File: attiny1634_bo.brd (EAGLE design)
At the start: 49.5 x 22.2 mm, 13 parts, among them J1 AVR_SPI_PRG_6NS, Y1 12MHz

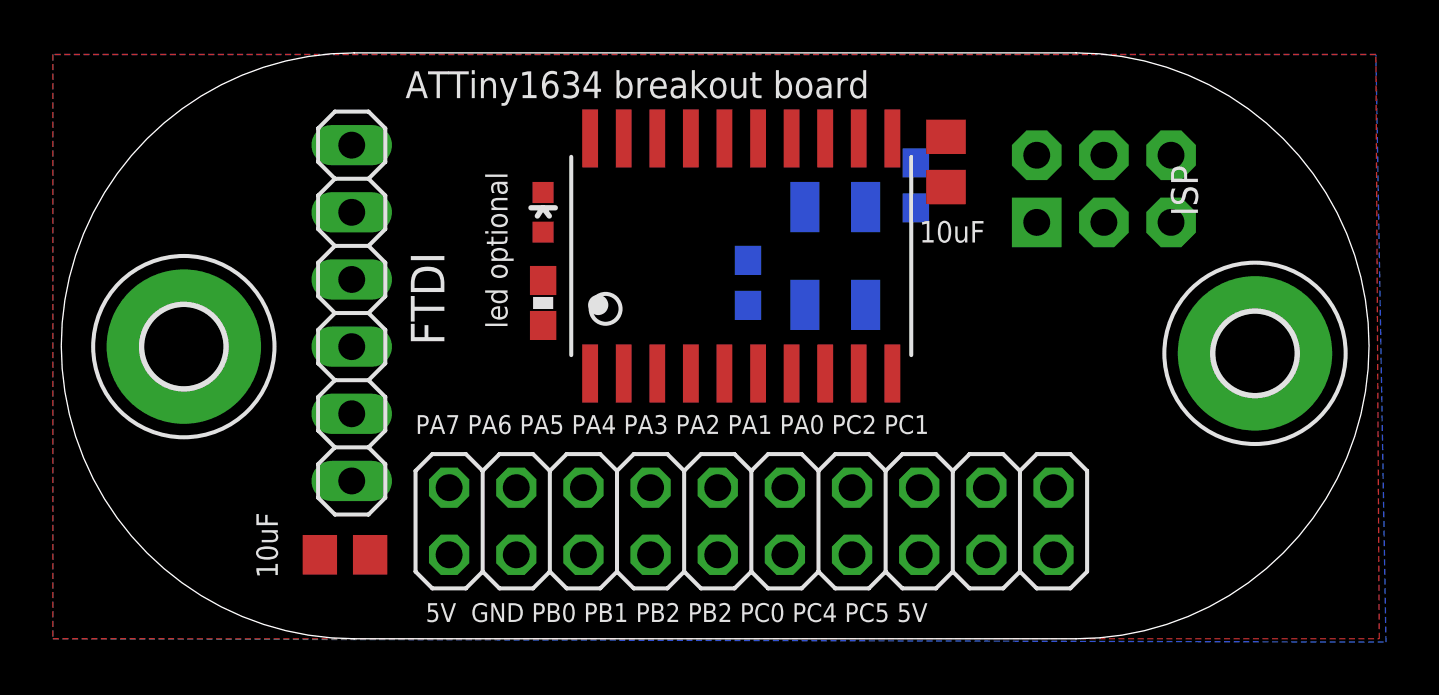
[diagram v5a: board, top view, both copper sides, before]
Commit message: added Arduino style FTDI UART header
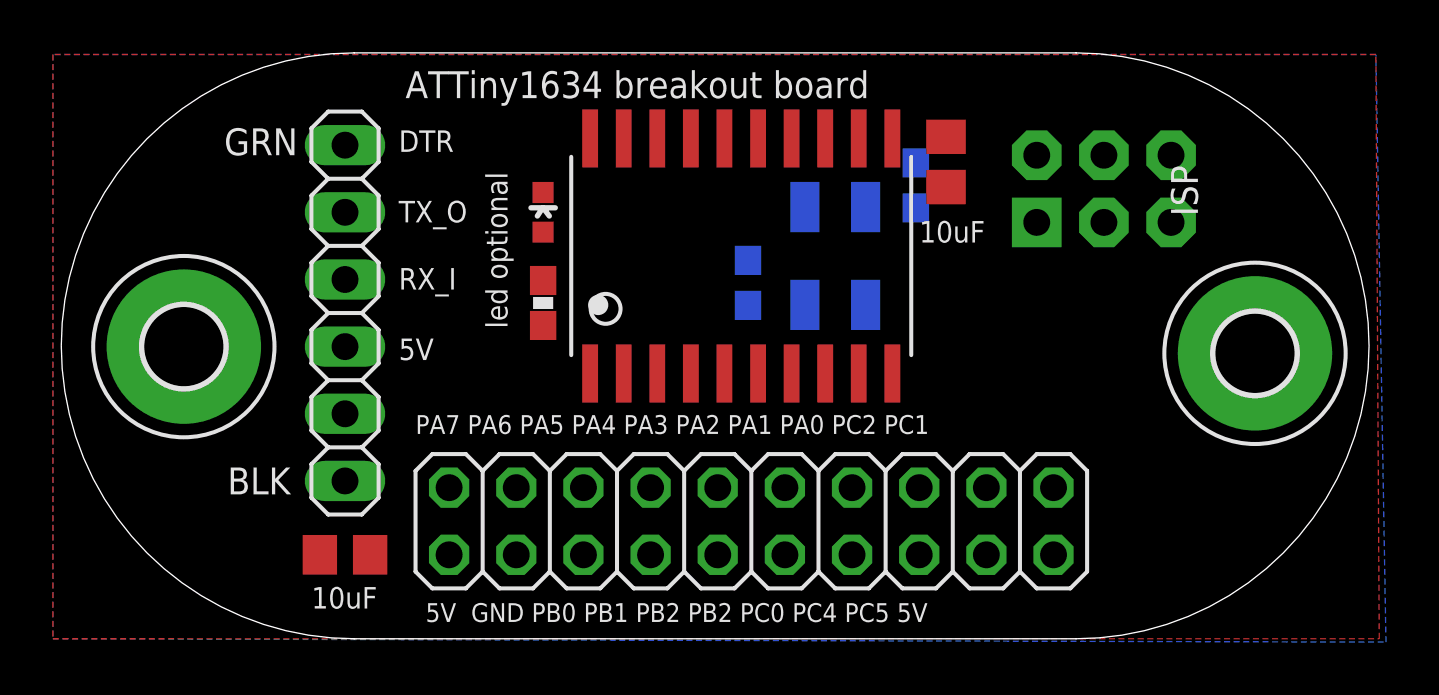
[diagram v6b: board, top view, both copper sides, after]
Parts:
- moved FTDI 0.25 mm to (11.0, 12.3)
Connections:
- removed net PA7: JP1.19
- new net CTS: FTDI.2
- new net PA7/RX0: FTDI.4, JP1.19
- net +5V: now also FTDI.3
- net GND: now also FTDI.1
- net PB0/TXD0: now also FTDI.5
- net PC3/-RESET: now also FTDI.6
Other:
- board text added: "5V"
- board text added: "BLK"
- board text added: "DTR"
- board text added: "GRN"
- board text added: "RX_I"
- board text added: "TX_O"
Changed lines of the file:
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@@
 <text x="27.432" y="16.51" size="0.8128" layer="26" font="vector" ratio="10" rot="MR0">XTAL optional (12MHz)</text>
 <text x="16.383" y="17.653" size="0.8128" layer="25" font="vector" ratio="10" rot="R270">led optional</text>
-<text x="8.509" y="2.286" size="0.8128" layer="25" font="vector" ratio="10" rot="R90">10uF</text>
+<text x="9.779" y="1.143" size="0.8128" layer="25" font="vector" ratio="10">10uF</text>
 <text x="32.766" y="14.986" size="0.8128" layer="25" font="vector" ratio="10">10uF</text>
 <text x="25.781" y="15.367" size="0.8128" layer="26" ratio="10" rot="MR0">12pF caps for xtal</text>
 <circle x="20.6248" y="12.6238" radius="0.179603125" width="0.4064" layer="25"/>
+<text x="6.477" y="18.288" size="1.016" layer="25" ratio="10">GRN</text>
+<text x="6.604" y="5.461" size="1.016" layer="25" ratio="10">BLK</text>
+<text x="13.081" y="18.415" size="0.8128" layer="25" ratio="10">DTR</text>
+<text x="13.081" y="15.748" size="0.8128" layer="25" ratio="10">TX_O</text>
+<text x="13.081" y="13.208" size="0.8128" layer="25" ratio="10">RX_I</text>
+<text x="13.081" y="10.541" size="0.8128" layer="25" ratio="10">5V</text>
 </plain>
 <attributes>
@@
 <element name="U$1" library="attiny1634" package="SOIC20" value="ATTINY1634" x="22.225" y="14.478" smashed="yes"/>
 <element name="RLED1" library="SparkFun-Passives" package="0603-RES" value="330" x="18.542" y="12.7" smashed="yes" rot="R270"/>
-<element name="FTDI" library="pinhead" package="1X06" value="" x="11.303" y="12.319" smashed="yes" rot="R90">
-<attribute name="NAME" x="14.8082" y="11.0998" size="1.27" layer="25" ratio="10" rot="R90"/>
-<attribute name="VALUE" x="14.478" y="4.699" size="1.27" layer="27" rot="R90"/>
+<element name="FTDI" library="pinhead" package="1X06" value="" x="11.049" y="12.319" smashed="yes" rot="R90">
+<attribute name="VALUE" x="14.224" y="4.699" size="1.27" layer="27" rot="R90"/>
 </element>
 </elements>
@@
 <contactref element="U$1" pad="10"/>
 <contactref element="U$1" pad="10"/>
+<contactref element="FTDI" pad="1"/>
 </signal>
 <signal name="+5V" class="1">
@@
 <contactref element="U$1" pad="11"/>
 <contactref element="RLED1" pad="2"/>
+<contactref element="FTDI" pad="3"/>
 <wire x1="33.782" y1="18.984" x2="37.211" y2="18.288" width="0" layer="19" extent="1-1"/>
 <wire x1="31.75" y1="18.923" x2="33.782" y2="18.984" width="0" layer="19" extent="1-1"/>
 <wire x1="18.542" y1="11.85" x2="31.75" y2="18.923" width="0" layer="19" extent="1-1"/>
-<wire x1="14.986" y1="3.175" x2="18.542" y2="11.85" width="0" layer="19" extent="1-1"/>
-<wire x1="11.999" y1="3.175" x2="14.986" y2="3.175" width="0" layer="19" extent="1-1"/>
+<wire x1="11.049" y1="11.049" x2="18.542" y2="11.85" width="0" layer="19" extent="1-1"/>
+<wire x1="11.999" y1="3.175" x2="11.049" y2="11.049" width="0" layer="19" extent="1-1"/>
+<wire x1="14.986" y1="3.175" x2="11.999" y2="3.175" width="0" layer="19" extent="1-1"/>
 <wire x1="37.846" y1="3.175" x2="37.211" y2="18.288" width="0" layer="19" extent="1-1"/>
 </signal>
@@
 <contactref element="J1" pad="5"/>
 <contactref element="U$1" pad="14"/>
+<contactref element="FTDI" pad="6"/>
 <wire x1="27.94" y1="18.923" x2="42.291" y2="15.748" width="0" layer="19" extent="1-1"/>
+<wire x1="11.049" y1="18.669" x2="27.94" y2="18.923" width="0" layer="19" extent="1-1"/>
 </signal>
 <signal name="PC5/XTAL1">
@@
 <contactref element="JP1" pad="9"/>
 </signal>
-<signal name="PA7">
+<signal name="PA7/RX0">
 <contactref element="JP1" pad="19"/>
+<contactref element="FTDI" pad="4"/>
+<wire x1="14.986" y1="5.715" x2="11.049" y2="13.589" width="0" layer="19" extent="1-1"/>
 </signal>
 <signal name="PA6">
@@
 <signal name="PB0/TXD0">
 <contactref element="U$1" pad="1"/>
+<contactref element="FTDI" pad="5"/>
+<wire x1="11.049" y1="16.129" x2="20.32" y2="10.033" width="0" layer="19" extent="1-1"/>
 </signal>
 <signal name="PB1/MOSI/ADC6">
@@
 <wire x1="18.542" y1="13.55" x2="18.542" y2="15.379" width="0" layer="19" extent="1-1"/>
 </signal>
+<signal name="CTS">
+<contactref element="FTDI" pad="2"/>
+</signal>
 </signals>

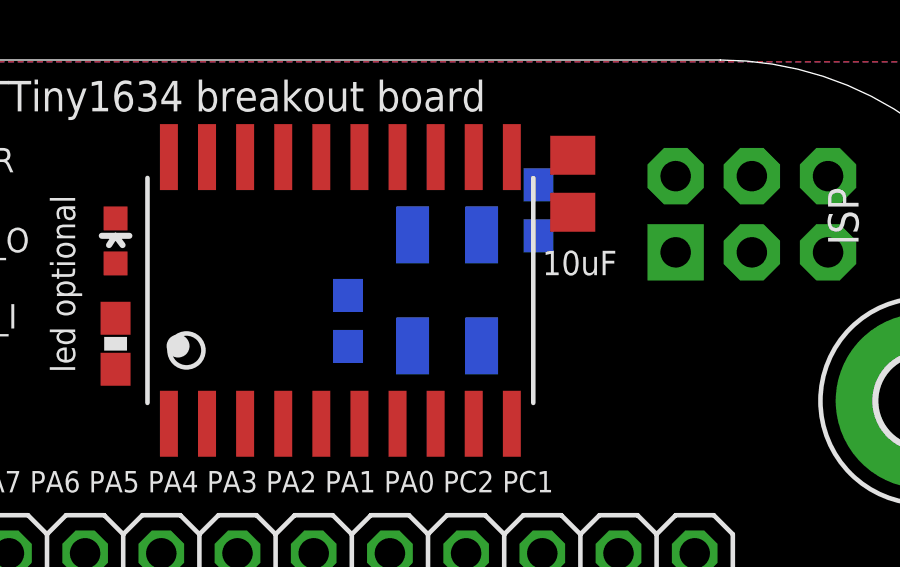
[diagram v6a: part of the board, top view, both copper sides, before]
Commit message: manually routed the xtal
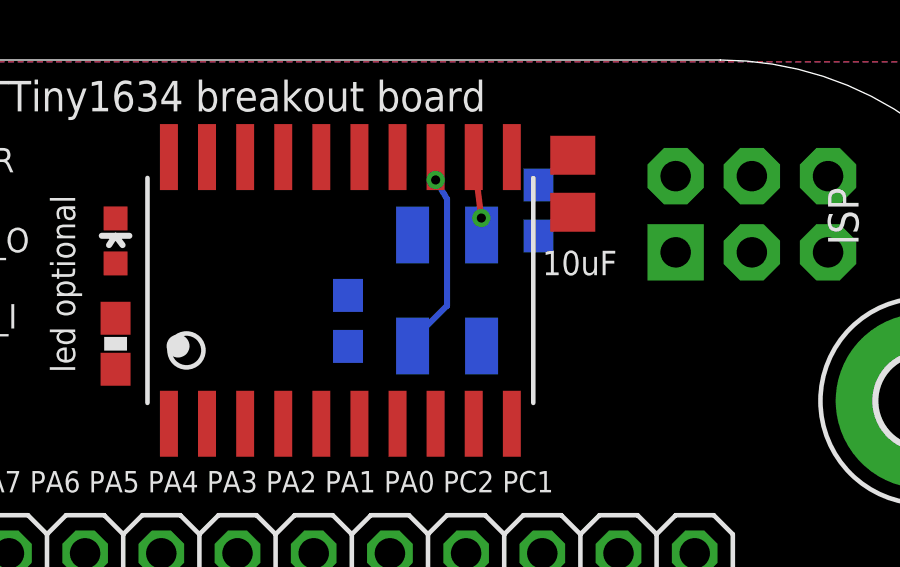
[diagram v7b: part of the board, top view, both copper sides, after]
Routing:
- net PC4/XTAL2: track 0.00 -> 6.88 mm, vias 0 -> 1
- net PC5/XTAL1: track 0.00 -> 2.81 mm, vias 0 -> 1
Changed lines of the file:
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@@
 <contactref element="JP1" pad="4"/>
 <contactref element="U$1" pad="12"/>
-<wire x1="30.741" y1="16.328" x2="30.48" y2="18.923" width="0" layer="19" extent="1-16"/>
-<wire x1="32.639" y1="16.295" x2="30.741" y2="16.328" width="0" layer="19" extent="16-16"/>
+<wire x1="30.48" y1="18.923" x2="30.734" y2="16.891" width="0.2032" layer="1"/>
+<via x="30.734" y="16.891" extent="1-16" drill="0.3048"/>
+<wire x1="30.734" y1="16.891" x2="30.48" y2="16.589" width="0.2032" layer="16"/>
+<wire x1="30.48" y1="16.589" x2="30.741" y2="16.328" width="0.2032" layer="16"/>
+<wire x1="30.741" y1="16.328" x2="32.639" y2="16.295" width="0" layer="19" extent="16-16"/>
 <wire x1="35.306" y1="3.175" x2="32.639" y2="16.295" width="0" layer="19" extent="16-16"/>
 </signal>
@@
 <contactref element="JP1" pad="6"/>
 <contactref element="U$1" pad="13"/>
-<wire x1="28.441" y1="12.628" x2="29.21" y2="18.923" width="0" layer="19" extent="1-16"/>
-<wire x1="26.289" y1="12.612" x2="28.441" y2="12.628" width="0" layer="19" extent="16-16"/>
+<wire x1="28.441" y1="12.628" x2="28.441" y2="12.82" width="0.2032" layer="16"/>
+<wire x1="28.441" y1="12.82" x2="29.591" y2="13.97" width="0.2032" layer="16"/>
+<wire x1="29.591" y1="13.97" x2="29.591" y2="17.526" width="0.2032" layer="16"/>
+<wire x1="29.591" y1="17.526" x2="29.21" y2="18.161" width="0.2032" layer="16"/>
+<wire x1="29.21" y1="18.923" x2="29.21" y2="18.161" width="0.2032" layer="1"/>
+<via x="29.21" y="18.161" extent="1-16" drill="0.3048"/>
+<wire x1="26.289" y1="12.612" x2="28.441" y2="12.82" width="0" layer="19" extent="16-16"/>
 <wire x1="32.766" y1="3.175" x2="28.441" y2="12.628" width="0" layer="19" extent="16-16"/>
 </signal>

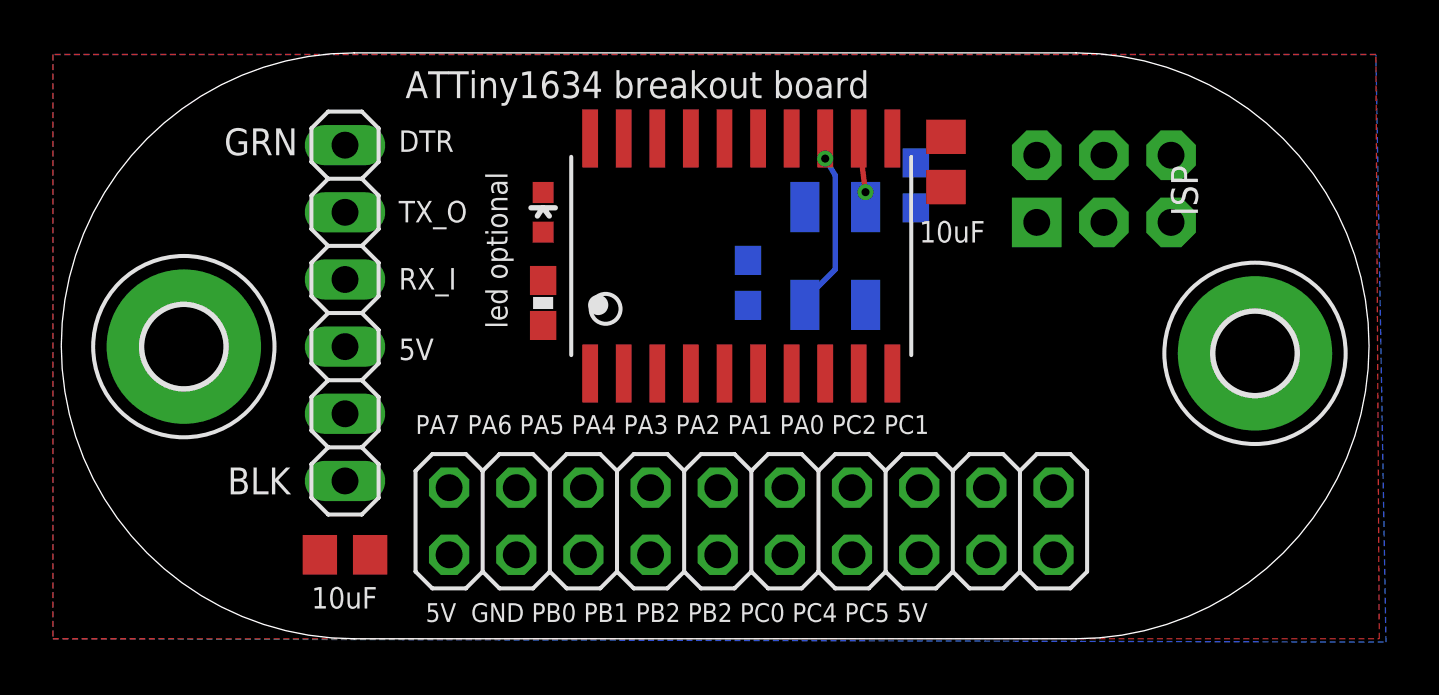
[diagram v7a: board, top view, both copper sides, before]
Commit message: Eagle autorouted
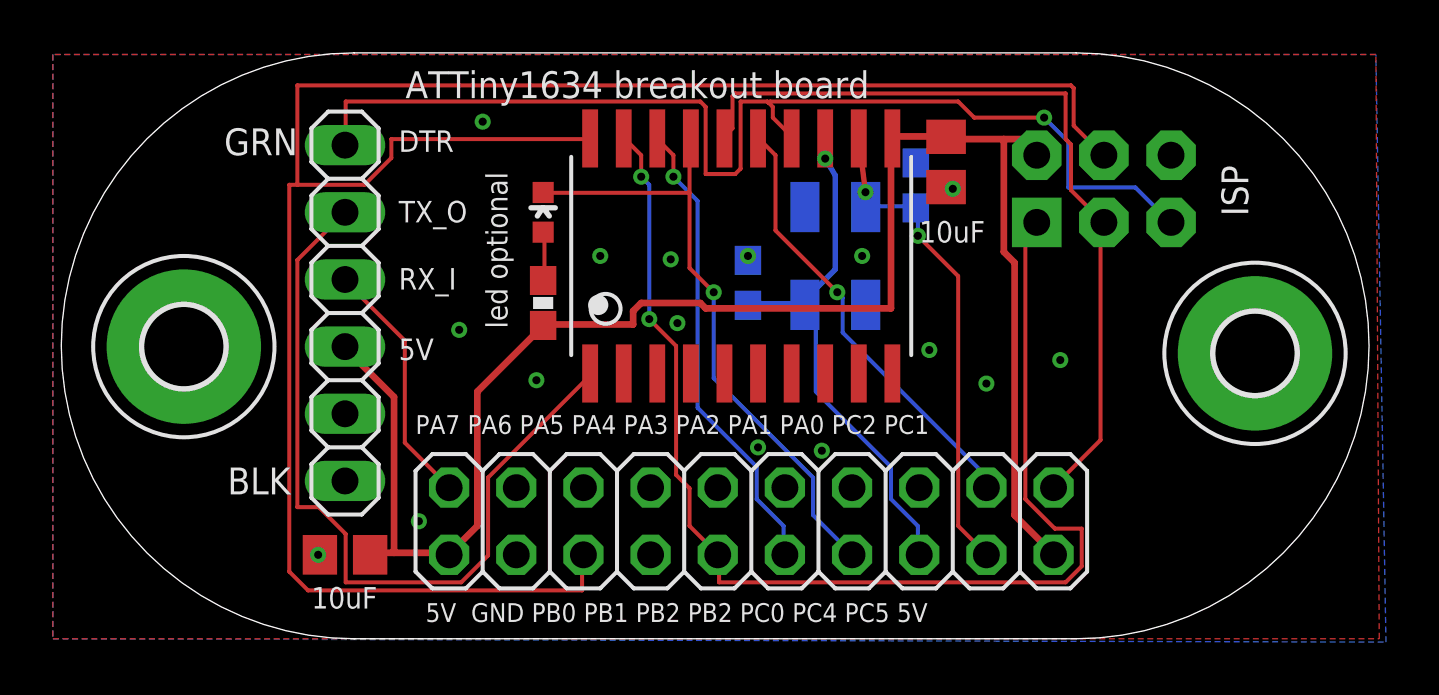
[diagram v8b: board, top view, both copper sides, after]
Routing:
- net PB1/MOSI/ADC6: track 0.00 -> 76.1 mm
- net +5V: track 0.00 -> 64.8 mm
- net PB2/ADC7/TX1: track 0.00 -> 46.9 mm, vias 0 -> 2
- net PC3/-RESET: track 0.00 -> 42.8 mm, vias 0 -> 1
- net PC1/SCL/ADC10: track 0.00 -> 30.7 mm
- net PB0/TXD0: track 0.00 -> 30.3 mm
- net PC0/ADC9/OC0A: track 0.00 -> 23.9 mm, vias 0 -> 1
- net PB3/ADC8/OC1A: track 0.00 -> 17.7 mm, vias 0 -> 1
- net PC2/ADC11: track 0.00 -> 16.8 mm, vias 0 -> 1
- net PC5/XTAL1: track 2.81 -> 19.0 mm, vias 1 -> 2
- net PC4/XTAL2: track 6.88 -> 20.4 mm
- net PA7/RX0: track 0.00 -> 9.49 mm
- net N$1: track 0.00 -> 1.87 mm
